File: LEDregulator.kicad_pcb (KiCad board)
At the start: 2 copper layers, 23 parts, among them J1 2.1mm DC jack, J2 2way Screw Terminal, J3 2way Screw Terminal

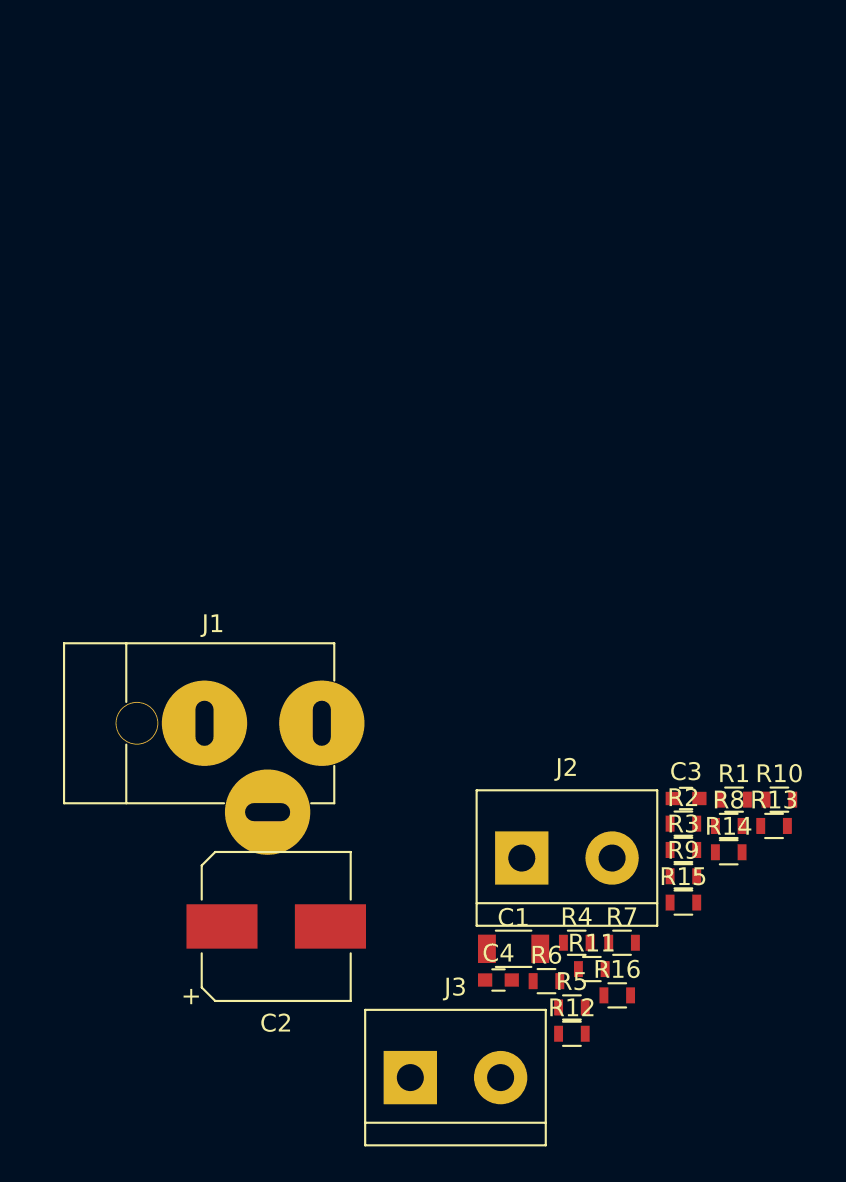
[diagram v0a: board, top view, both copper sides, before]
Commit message: Laid out PCB components
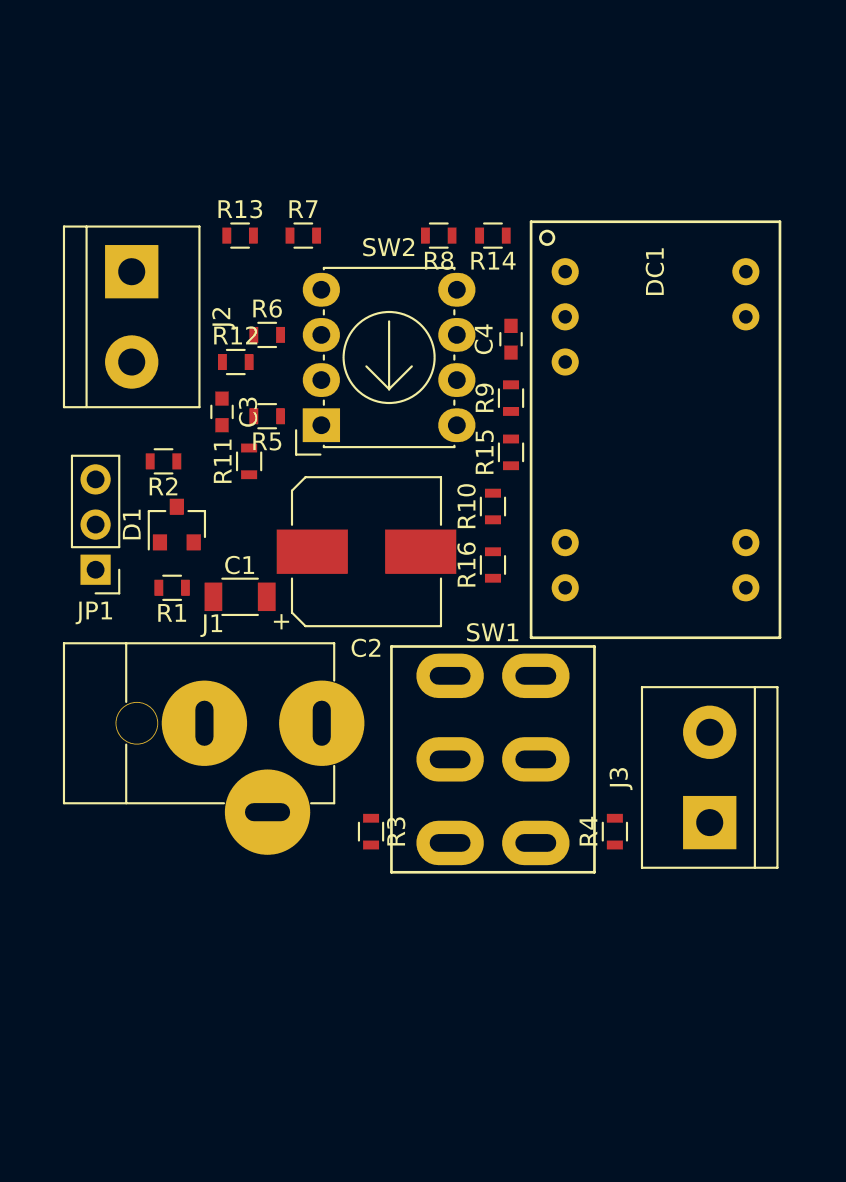
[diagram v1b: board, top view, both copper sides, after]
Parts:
- added D1: MAX6006, TO_SOT_Packages_SMD:SOT-23, F.Cu at (126.0, 65.5)
- added DC1: LED driver 24V/1A, jakub:XPPOWER_LDU24, F.Cu at (147.8, 51.3)
- added JP1: Jumper_3_Bridged12, Pin_Headers:Pin_Header_Straight_1x03_Pitch2.54mm, F.Cu at (121.4, 68.1)
- added SW1: DPDT Switch, jakub:switchDPDT, F.Cu at (143.8, 78.7)
- added SW2: 6pos rotary, jakub:Nidec_Copal_SS-10-16, F.Cu at (134.1, 52.3)
- moved R13 44.8 mm to (129.5, 49.3)
- moved R7 43.6 mm to (133.1, 49.3)
- moved R12 42.3 mm to (129.3, 56.4)
- moved J2 39.6 mm to (123.4, 51.3), turned to 270 degrees
- moved R6 39.6 mm to (131.1, 54.9)
- moved R5 37.4 mm to (131.1, 59.4), turned to 180 degrees
- moved R14 37.1 mm to (143.8, 49.3), turned to 180 degrees
- moved R8 37.0 mm to (140.7, 49.3), turned to 180 degrees
- moved C4 36.0 mm to (144.8, 55.1), turned to 90 degrees
- moved R2 35.6 mm to (125.2, 62.0), turned to 180 degrees
- moved R11 34.5 mm to (130.0, 62.0), turned to 90 degrees
- moved C3 34.0 mm to (128.5, 59.2), turned to 270 degrees
- moved R1 33.8 mm to (125.7, 69.1), turned to 180 degrees
- moved R9 28.6 mm to (144.8, 58.4), turned to 90 degrees
- moved R15 27.1 mm to (144.8, 61.5), turned to 90 degrees
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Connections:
- J1 pad 1: (no net) -> /+24V
- J2 pad 1: (no net) -> /ExtCtrl
- J3 pad 1: (no net) -> /LEDout
- R1 pad 2: (no net) -> /Vref
- R10 pad 2: (no net) -> /0.30V
- R3 pad 2: (no net) -> /+24V_TrickleSupply
- R4 pad 1: (no net) -> /TrickleOut
- R5 pad 2: (no net) -> /1.09V
- R6 pad 2: (no net) -> /0.93V
- R7 pad 2: (no net) -> /0.78V
- R8 pad 2: (no net) -> /0.62V
- R9 pad 2: (no net) -> /0.46V

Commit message: Laid out the PCB
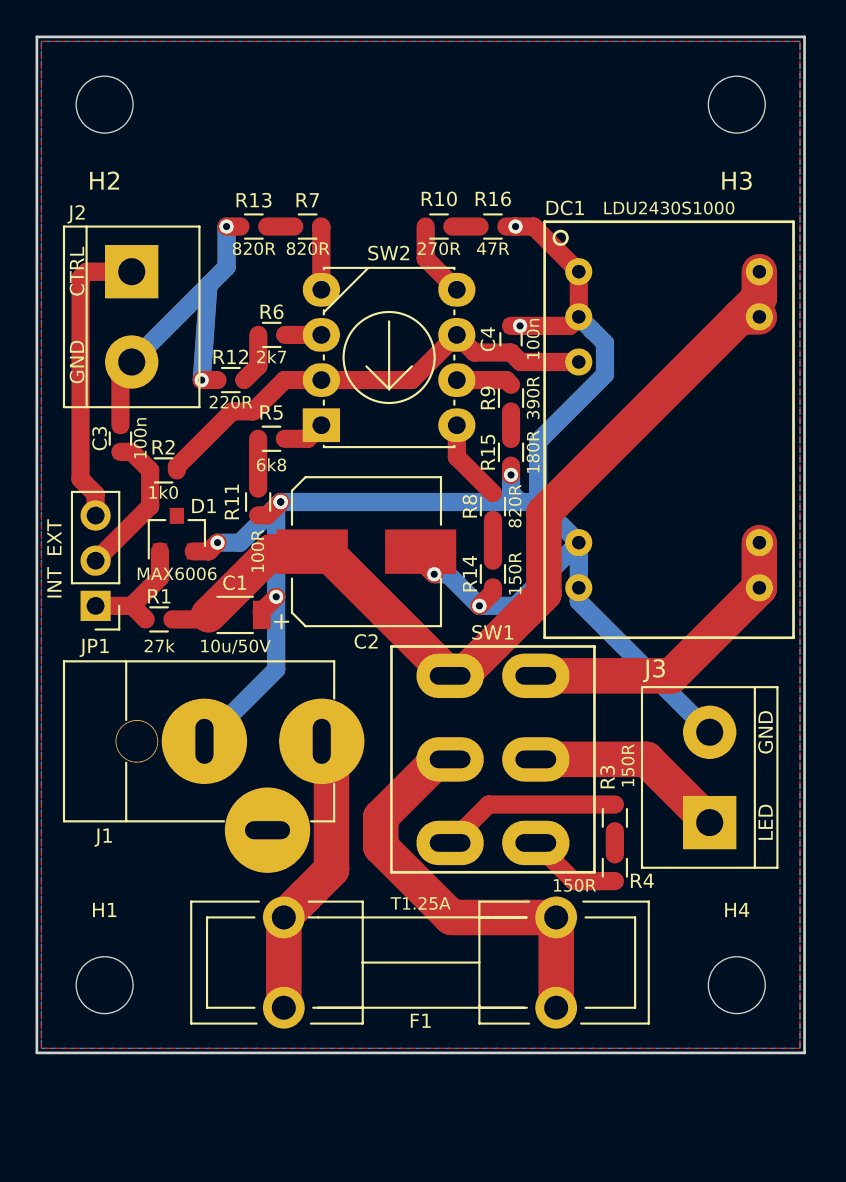
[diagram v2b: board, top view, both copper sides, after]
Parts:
- added F1: T1.25A, Fuse_Holders_and_Fuses:Fuseholder5x20_horiz_open_lateral_Type-II, F.Cu at (147.3, 92.7)
- added H1: ⌀3.2mm, Mounting_Holes:MountingHole_3.2mm_M3, F.Cu at (121.9, 91.4)
- added H2: ⌀3.2mm, Mounting_Holes:MountingHole_3.2mm_M3, F.Cu at (121.9, 41.9)
- added H3: ⌀3.2mm, Mounting_Holes:MountingHole_3.2mm_M3, F.Cu at (157.5, 41.9)
- added H4: ⌀3.2mm, Mounting_Holes:MountingHole_3.2mm_M3, F.Cu at (157.5, 91.4)
- DC1: value LED driver 24V/1A -> LDU2430S1000
- moved R16 19.0 mm to (143.8, 48.8), turned to 180 degrees
- moved R14 19.0 mm to (143.8, 68.3), turned to 90 degrees
- moved R10 16.0 mm to (140.7, 48.8), turned to 180 degrees
- moved R8 15.5 mm to (143.8, 64.5), turned to 90 degrees
- moved R3 13.7 mm to (150.6, 82.0), turned to 90 degrees
- moved C3 5.91 mm to (122.8, 60.7), turned to 90 degrees
- moved R11 2.34 mm to (130.6, 64.3)
- moved JP1 2.03 mm to (121.4, 70.1)
- moved R4 2.03 mm to (150.6, 84.8)
- moved R1 1.93 mm to (125.0, 70.9)
- moved R5 1.29 mm to (131.3, 60.7), turned to 0 degrees
- moved R12 1.05 mm to (129.0, 57.4)
- moved C1 1.05 mm to (129.3, 70.6)
- moved J1 1.02 mm to (119.6, 77.7)
- moved R13 0.93 mm to (130.3, 48.8)
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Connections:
- SW1 pad 2: /+24V -> Net-(F1-Pad1)
- SW2 pad 6: /CtrlVolt -> /0.46V
- SW2 pad 7: /0.46V -> /CtrlVolt
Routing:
- net GND: track 0.00 -> 116.1 mm, vias 0 -> 12
- net /+24V_DriverSupply: track 0.00 -> 51.5 mm
- net /CtrlVolt: track 0.00 -> 26.5 mm
- net Net-(F1-Pad1): track 0.00 -> 23.9 mm
- net /DriverOut: track 0.00 -> 17.2 mm
- net /ExtCtrl: track 0.00 -> 16.7 mm
- net /+24V: track 0.00 -> 16.3 mm
- net /LEDout: track 0.00 -> 11.3 mm
- net /+24V_TrickleSupply: track 0.00 -> 10.2 mm
- net /RefVolt: track 0.00 -> 8.46 mm
- net /Vref: track 0.00 -> 6.85 mm
- net /TrickleOut: track 0.00 -> 5.34 mm
- net /0.62V: track 0.00 -> 4.66 mm
- net /0.30V: track 0.00 -> 4.28 mm
- net /0.78V: track 0.00 -> 3.57 mm
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- added copper zone on B.Cu, net GND
- added copper zone on F.Cu, net GND
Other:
- board outline added: 43.2 x 57.1 mm
- board text added: "CTRL"
- board text added: "EXT"
- board text added: "GND"
- board text added: "INT"
- board text added: "LED"

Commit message: Board ready
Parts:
- added R5: 120R, Resistors_SMD:R_0603, F.Cu at (154.2, 87.1)
- R3, R4: value 150R -> 120R
- moved C1 0.23 mm to (129.0, 70.6)
- renumbered R9 to R10, R10 to R11, R11 to R12, R12 to R13, R13 to R14, R14 to R15, R15 to R16, R16 to R17, R5 to R6, R6 to R7, R7 to R8, R8 to R9
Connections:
- R4 pad 1: /TrickleOut -> Net-(R4-Pad1)
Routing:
- net Net-(R4-Pad1): track 0.00 -> 5.82 mm
- net /TrickleOut: track 5.34 -> 8.79 mm
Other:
- board text added: "2:74% 3:62%"
- board text added: "4:49% 5:36%"
- board text added: "6:24%"
- board text added: "LED driver v1.0 Jakub Nedbal, 2019"
- board text added: "·:100% 1:87%"

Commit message: Initial commit. Sent for manufacture.
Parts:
- added REF**: Symbol_CC-ShareAlike_CopperTop_Small, Symbol:Symbol_CC-ShareAlike_CopperTop_Small, B.Cu at (130.6, 41.9)
- added REF**: Symbol_CC-Attribution_CopperTop_Small, Symbol:Symbol_CC-Attribution_CopperTop_Small, B.Cu at (136.7, 41.9)
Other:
- board text added: "CC-BY-SA"
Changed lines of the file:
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@@
   (general
     (thickness 1.6)
-    (drawings 19)
+    (drawings 20)
     (tracks 142)
     (zones 0)
-    (modules 34)
+    (modules 36)
     (nets 27)
   )
   (page A4)
   (layers
-    (0 F.Cu signal hide)
-    (31 B.Cu signal hide)
+    (0 F.Cu signal)
+    (31 B.Cu signal)
     (32 B.Adhes user)
     (33 F.Adhes user)
@@
     (add_net "Net-(R4-Pad1)")
   )
+  (module Symbol:Symbol_CC-ShareAlike_CopperTop_Small (layer B.Cu)
+    (at 130.556 41.91 180)
+    (descr "Symbol, CC-Share Alike, Copper Top, Small,")
+    (tags "Symbol, CC-Share Alike, Copper Top, Small,")
+    (attr virtual)
+    (fp_text reference REF** (at 0.59944 7.29996) (layer B.SilkS) hide
+      (effects (font (size 1 1) (thickness 0.15)) (justify mirror))
+    )
+    (fp_text value Symbol_CC-ShareAlike_CopperTop_Small (at 1.016 -7.874) (layer B.Fab) hide
+      (effects (font (size 1 1) (thickness 0.15)) (justify mirror))
+    )
+    (fp_line (start 0.59944 2.4003) (end 0 2.49936) (layer B.Cu) (width 0.381))
+    (fp_line (start 1.00076 2.30124) (end 0.59944 2.4003) (layer B.Cu) (width 0.381))
+    (fp_line (start 1.50114 1.99898) (end 1.00076 2.30124) (layer B.Cu) (width 0.381))
+    (fp_line (start 1.99898 1.50114) (end 1.50114 1.99898) (layer B.Cu) (width 0.381))
+    (fp_line (start 2.30124 1.00076) (end 1.99898 1.50114) (layer B.Cu) (width 0.381))
+    (fp_line (start 2.49936 0.39878) (end 2.30124 1.00076) (layer B.Cu) (width 0.381))
+    (fp_line (start 2.49936 -0.20066) (end 2.49936 0.39878) (layer B.Cu) (width 0.381))
+    (fp_line (start 2.4003 -0.8001) (end 2.49936 -0.20066) (layer B.Cu) (width 0.381))
+    (fp_line (start 1.99898 -1.50114) (end 2.4003 -0.8001) (layer B.Cu) (width 0.381))
+    (fp_line (start 1.50114 -1.99898) (end 1.99898 -1.50114) (layer B.Cu) (width 0.381))
+    (fp_line (start 0.89916 -2.30124) (end 1.50114 -1.99898) (layer B.Cu) (width 0.381))
+    (fp_line (start 0.29972 -2.49936) (end 0.89916 -2.30124) (layer B.Cu) (width 0.381))
+    (fp_line (start -0.50038 -2.49936) (end 0.29972 -2.49936) (layer B.Cu) (width 0.381))
+    (fp_line (start -1.19888 -2.19964) (end -0.50038 -2.49936) (layer B.Cu) (width 0.381))
+    (fp_line (start -1.69926 -1.80086) (end -1.19888 -2.19964) (layer B.Cu) (width 0.381))
+    (fp_line (start -2.30124 -1.09982) (end -1.69926 -1.80086) (layer B.Cu) (width 0.381))
+    (fp_line (start -2.49936 -0.29972) (end -2.30124 -1.09982) (layer B.Cu) (width 0.381))
+    (fp_line (start -2.49936 0.29972) (end -2.49936 -0.29972) (layer B.Cu) (width 0.381))
+    (fp_line (start -2.4003 0.8001) (end -2.49936 0.29972) (layer B.Cu) (width 0.381))
+    (fp_line (start -2.19964 1.19888) (end -2.4003 0.8001) (layer B.Cu) (width 0.381))
+    (fp_line (start -1.69926 1.80086) (end -2.19964 1.19888) (layer B.Cu) (width 0.381))
+    (fp_line (start -1.19888 2.19964) (end -1.69926 1.80086) (layer B.Cu) (width 0.381))
+    (fp_line (start -0.70104 2.4003) (end -1.19888 2.19964) (layer B.Cu) (width 0.381))
+    (fp_line (start -0.09906 2.49936) (end -0.70104 2.4003) (layer B.Cu) (width 0.381))
+    (fp_line (start 0 2.49936) (end -0.09906 2.49936) (layer B.Cu) (width 0.381))
+    (fp_line (start -0.50038 1.50114) (end -1.00076 1.30048) (layer B.Cu) (width 0.381))
+    (fp_line (start -0.09906 1.6002) (end -0.50038 1.50114) (layer B.Cu) (width 0.381))
+    (fp_line (start 0.29972 1.6002) (end -0.09906 1.6002) (layer B.Cu) (width 0.381))
+    (fp_line (start 0.89916 1.30048) (end 0.29972 1.6002) (layer B.Cu) (width 0.381))
+    (fp_line (start 1.19888 1.00076) (end 0.89916 1.30048) (layer B.Cu) (width 0.381))
+    (fp_line (start 1.50114 0.50038) (end 1.19888 1.00076) (layer B.Cu) (width 0.381))
+    (fp_line (start 1.6002 0) (end 1.50114 0.50038) (layer B.Cu) (width 0.381))
+    (fp_line (start 1.6002 -0.39878) (end 1.6002 0) (layer B.Cu) (width 0.381))
+    (fp_line (start 1.30048 -0.89916) (end 1.6002 -0.39878) (layer B.Cu) (width 0.381))
+    (fp_line (start 0.89916 -1.30048) (end 1.30048 -0.89916) (layer B.Cu) (width 0.381))
+    (fp_line (start 0.39878 -1.50114) (end 0.89916 -1.30048) (layer B.Cu) (width 0.381))
+    (fp_line (start -0.09906 -1.6002) (end 0.39878 -1.50114) (layer B.Cu) (width 0.381))
+    (fp_line (start -0.59944 -1.50114) (end -0.09906 -1.6002) (layer B.Cu) (width 0.381))
+    (fp_line (start -1.09982 -1.19888) (end -0.59944 -1.50114) (layer B.Cu) (width 0.381))
+  )
+  (module Symbol:Symbol_CC-Attribution_CopperTop_Small (layer B.Cu)
+    (at 136.652 41.91 180)
+    (descr "Symbol, CC-Share Alike, Copper Top, Small,")
+    (tags "Symbol, CC-Share Alike, Copper Top, Small,")
+    (attr virtual)
+    (fp_text reference REF** (at 0.59944 7.29996) (layer B.SilkS) hide
+      (effects (font (size 1 1) (thickness 0.15)) (justify mirror))
+    )
+    (fp_text value Symbol_CC-Attribution_CopperTop_Small (at 0.59944 -8.001) (layer B.Fab) hide
+      (effects (font (size 1 1) (thickness 0.15)) (justify mirror))
+    )
+    (fp_line (start 0.59944 2.4003) (end 0 2.49936) (layer B.Cu) (width 0.381))
+    (fp_line (start 1.00076 2.30124) (end 0.59944 2.4003) (layer B.Cu) (width 0.381))
+    (fp_line (start 1.50114 1.99898) (end 1.00076 2.30124) (layer B.Cu) (width 0.381))
+    (fp_line (start 1.99898 1.50114) (end 1.50114 1.99898) (layer B.Cu) (width 0.381))
+    (fp_line (start 2.30124 1.00076) (end 1.99898 1.50114) (layer B.Cu) (width 0.381))
+    (fp_line (start 2.49936 0.39878) (end 2.30124 1.00076) (layer B.Cu) (width 0.381))
+    (fp_line (start 2.49936 -0.20066) (end 2.49936 0.39878) (layer B.Cu) (width 0.381))
+    (fp_line (start 2.4003 -0.8001) (end 2.49936 -0.20066) (layer B.Cu) (width 0.381))
+    (fp_line (start 1.99898 -1.50114) (end 2.4003 -0.8001) (layer B.Cu) (width 0.381))
+    (fp_line (start 1.50114 -1.99898) (end 1.99898 -1.50114) (layer B.Cu) (width 0.381))
+    (fp_line (start 0.89916 -2.30124) (end 1.50114 -1.99898) (layer B.Cu) (width 0.381))
+    (fp_line (start 0.29972 -2.49936) (end 0.89916 -2.30124) (layer B.Cu) (width 0.381))
+    (fp_line (start -0.50038 -2.49936) (end 0.29972 -2.49936) (layer B.Cu) (width 0.381))
+    (fp_line (start -1.19888 -2.19964) (end -0.50038 -2.49936) (layer B.Cu) (width 0.381))
+    (fp_line (start -1.69926 -1.80086) (end -1.19888 -2.19964) (layer B.Cu) (width 0.381))
+    (fp_line (start -2.30124 -1.09982) (end -1.69926 -1.80086) (layer B.Cu) (width 0.381))
+    (fp_line (start -2.49936 -0.29972) (end -2.30124 -1.09982) (layer B.Cu) (width 0.381))
+    (fp_line (start -2.49936 0.29972) (end -2.49936 -0.29972) (layer B.Cu) (width 0.381))
+    (fp_line (start -2.4003 0.8001) (end -2.49936 0.29972) (layer B.Cu) (width 0.381))
+    (fp_line (start -2.19964 1.19888) (end -2.4003 0.8001) (layer B.Cu) (width 0.381))
+    (fp_line (start -1.69926 1.80086) (end -2.19964 1.19888) (layer B.Cu) (width 0.381))
+    (fp_line (start -1.19888 2.19964) (end -1.69926 1.80086) (layer B.Cu) (width 0.381))
+    (fp_line (start -0.70104 2.4003) (end -1.19888 2.19964) (layer B.Cu) (width 0.381))
+    (fp_line (start -0.09906 2.49936) (end -0.70104 2.4003) (layer B.Cu) (width 0.381))
+    (fp_line (start 0 2.49936) (end -0.09906 2.49936) (layer B.Cu) (width 0.381))
+    (fp_circle (center 0 1.69926) (end 0.09906 1.39954) (layer B.Cu) (width 0.381))
+    (fp_line (start -0.8001 -0.20066) (end -0.8001 1.00076) (layer B.Cu) (width 0.381))
+    (fp_line (start 0.70104 -0.20066) (end -0.8001 -0.20066) (layer B.Cu) (width 0.381))
+    (fp_line (start 0.70104 1.00076) (end 0.70104 -0.20066) (layer B.Cu) (width 0.381))
+    (fp_line (start -0.8001 1.00076) (end 0.70104 1.00076) (layer B.Cu) (width 0.381))
+    (fp_line (start -0.29972 -1.80086) (end 0.20066 -1.80086) (layer B.Cu) (width 0.381))
+    (fp_line (start -0.29972 -0.29972) (end -0.29972 -1.80086) (layer B.Cu) (width 0.381))
+    (fp_line (start 0.29972 -1.80086) (end 0.29972 -0.20066) (layer B.Cu) (width 0.381))
+    (fp_line (start 0.09906 -1.80086) (end 0.29972 -1.80086) (layer B.Cu) (width 0.381))
+    (fp_line (start 0 -0.29972) (end 0 -1.6002) (layer B.Cu) (width 0.381))
+    (fp_line (start -0.8001 0.09906) (end 0.50038 0.09906) (layer B.Cu) (width 0.381))
+    (fp_line (start 0.50038 0.39878) (end -0.70104 0.39878) (layer B.Cu) (width 0.381))
+    (fp_line (start -0.70104 0.70104) (end 0.59944 0.70104) (layer B.Cu) (width 0.381))
+    (fp_line (start 0 1.89992) (end 0 1.50114) (layer B.Cu) (width 0.381))
+  )
   (module jakub:Nidec_Copal_SS-10-16 (layer F.Cu)
     (at 134.112 52.324)
@@
     )
   )
+  (gr_text CC-BY-SA (at 133.604 46.736) (layer B.SilkS)
+    (effects (font (size 1 1) (thickness 0.15)) (justify mirror))
+  )
   (gr_text LED (at 160.655 82.296 90) (layer F.SilkS)
